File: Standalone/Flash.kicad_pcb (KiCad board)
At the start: 2 copper layers, 83.3 x 92.7 mm, 47 parts, among them CON1 GENESIS-CONN, J1 USB_B_Micro, U1 RT9193, U2 STM32F103C8Tx, U3 4069, U4 74HC590, U5 74LVC245, U6 74HC590, U7 74LVC245, U8 74HC590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

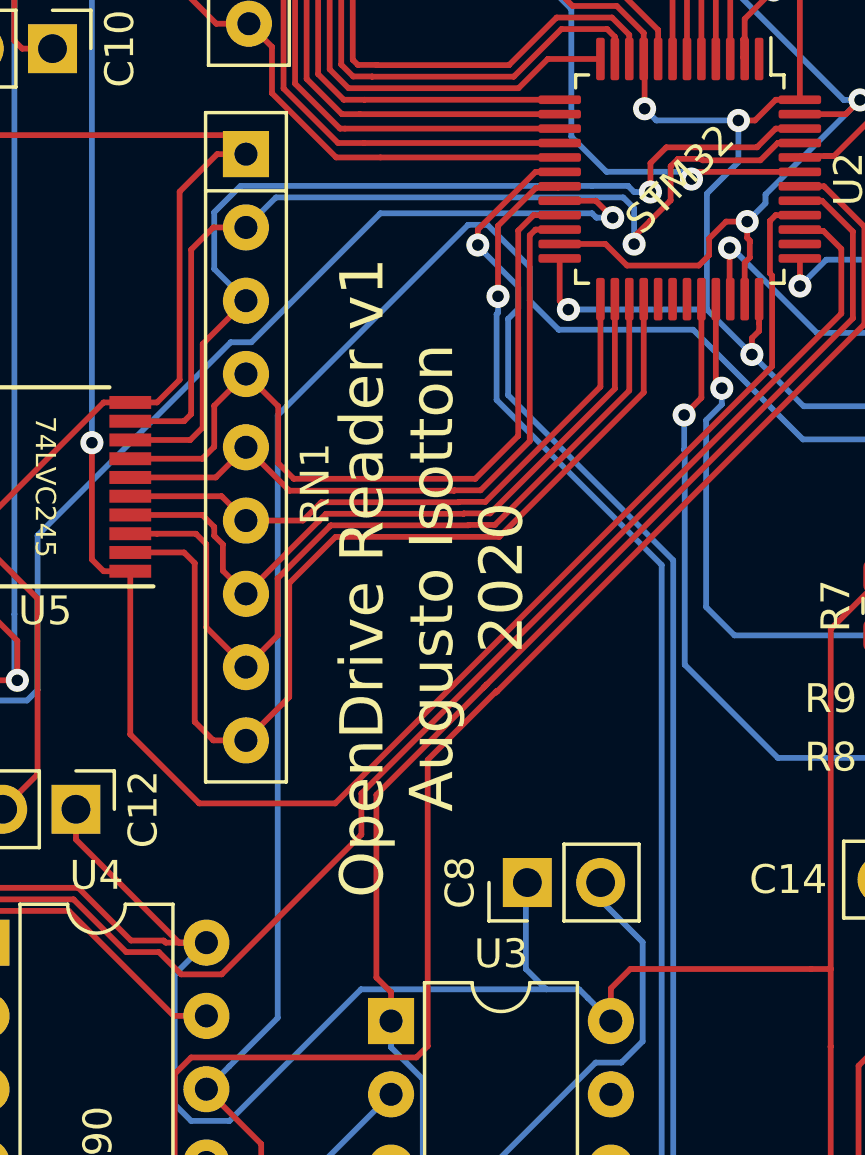
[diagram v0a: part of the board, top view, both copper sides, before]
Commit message: Small silkscreen changes
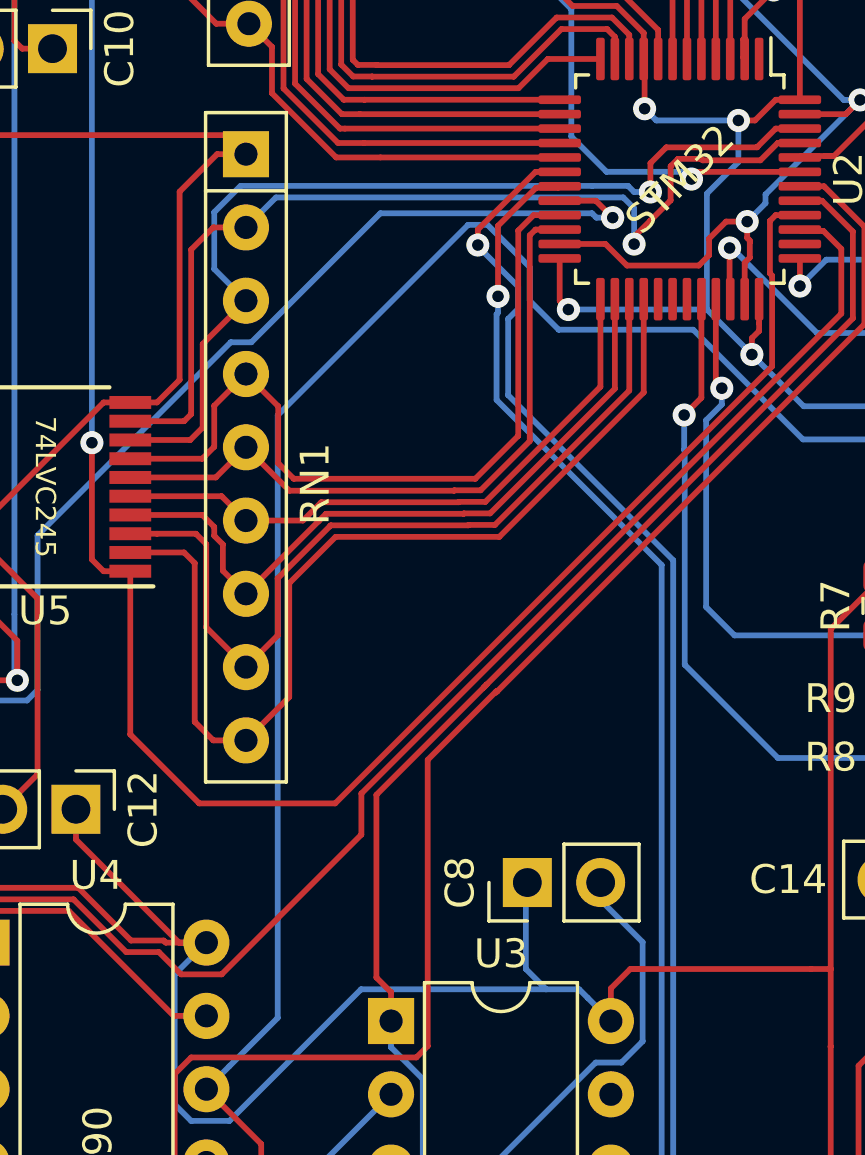
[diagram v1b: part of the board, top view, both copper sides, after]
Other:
- board text removed: "OpenDrive Reader v1 Augusto Isotton 2020"
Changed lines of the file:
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@@
   (general
     (thickness 1.6)
-    (drawings 28)
+    (drawings 27)
     (tracks 1703)
     (zones 0)
@@
     (effects (font (size 1 1) (thickness 0.15)))
   )
-  (gr_text "OpenDrive Reader v1\nAugusto Isotton\n2020" (at 136.5504 63.754 90) (layer F.SilkS)
-    (effects (font (size 1.5 1.5) (thickness 0.3)))
-  )
   (gr_text "GND\n" (at 98.6536 43.8912 90) (layer F.SilkS)

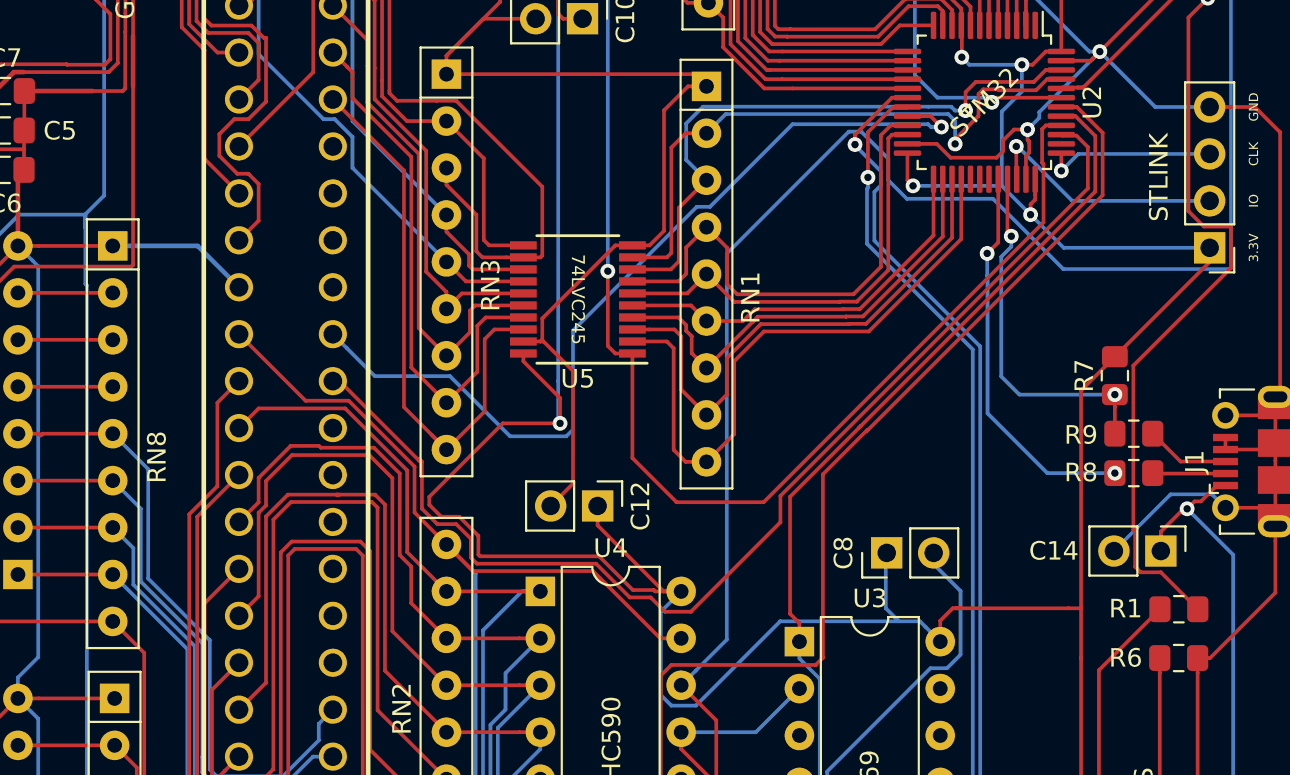
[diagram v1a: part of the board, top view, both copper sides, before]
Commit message: Connected A22 and A23 on the cart connector for SNES support
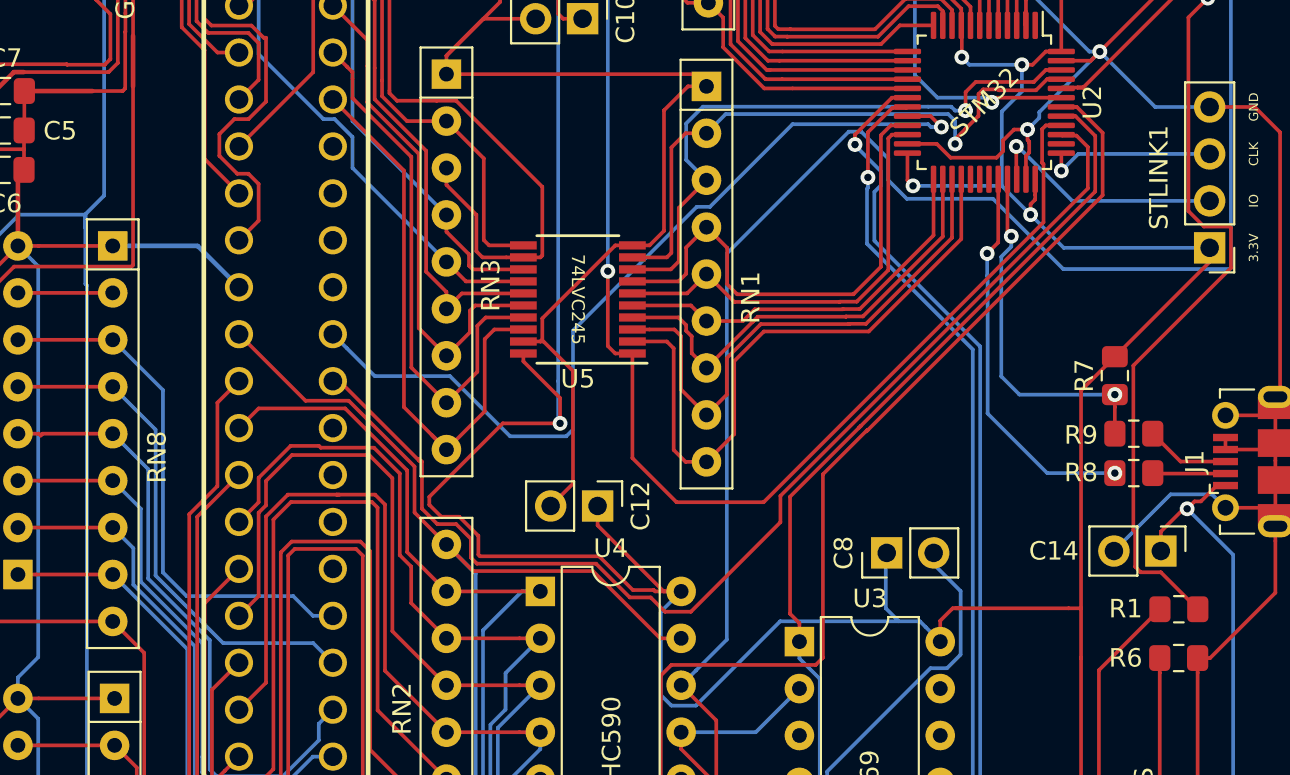
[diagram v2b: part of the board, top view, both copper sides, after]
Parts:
- renumbered STLINK to STLINK1
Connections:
- CON1 pad B10: (no net) -> /A21
- CON1 pad B11: (no net) -> /A22
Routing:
- net /A22: track 5.08 -> 29.0 mm
- net /A21: track 5.08 -> 27.8 mm
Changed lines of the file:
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@@
     (thickness 1.6)
     (drawings 27)
-    (tracks 1703)
+    (tracks 1714)
     (zones 0)
     (modules 47)
@@
   )
   (setup
-    (last_trace_width 0.25)
+    (last_trace_width 0.2)
     (user_trace_width 0.2)
     (user_trace_width 0.5)
@@
     (pad B9 thru_hole circle (at 0 20.32) (size 1.524 1.524) (drill 1.016) (layers *.Cu *.Mask)
       (net 28 /A20))
-    (pad B10 thru_hole circle (at 0 22.86) (size 1.524 1.524) (drill 1.016) (layers *.Cu *.Mask))
-    (pad B11 thru_hole circle (at 0 25.4) (size 1.524 1.524) (drill 1.016) (layers *.Cu *.Mask))
+    (pad B10 thru_hole circle (at 0 22.86) (size 1.524 1.524) (drill 1.016) (layers *.Cu *.Mask)
+      (net 76 /A21))
+    (pad B11 thru_hole circle (at 0 25.4) (size 1.524 1.524) (drill 1.016) (layers *.Cu *.Mask)
+      (net 77 /A22))
     (pad B12 thru_hole circle (at 0 27.94) (size 1.524 1.524) (drill 1.016) (layers *.Cu *.Mask))
     (pad B13 thru_hole circle (at 0 30.48) (size 1.524 1.524) (drill 1.016) (layers *.Cu *.Mask))
@@
     (descr "Through hole straight pin header, 1x04, 2.54mm pitch, single row")
     (tags "Through hole pin header THT 1x04 2.54mm single row")
-    (fp_text reference STLINK (at 2.7432 3.81 90) (layer F.SilkS)
+    (fp_text reference STLINK1 (at 2.7432 3.81 90) (layer F.SilkS)
       (effects (font (size 1 1) (thickness 0.15)))
     )
@@
   (segment (start 139.18561 57.42591) (end 144.908411 63.148711) (width 0.2) (layer B.Cu) (net 75))
   (segment (start 92.837 65.3288) (end 97.917 65.3288) (width 0.2) (layer F.Cu) (net 76) (status 30))
+  (segment (start 108.818399 79.201999) (end 109.8804 80.264) (width 0.2) (layer B.Cu) (net 76))
+  (segment (start 103.943792 79.201999) (end 108.818399 79.201999) (width 0.2) (layer B.Cu) (net 76))
+  (segment (start 100.28543 75.543637) (end 103.943792 79.201999) (width 0.2) (layer B.Cu) (net 76))
+  (segment (start 97.9678 65.3288) (end 100.28543 67.64643) (width 0.2) (layer B.Cu) (net 76))
+  (segment (start 100.28543 67.64643) (end 100.28543 75.543637) (width 0.2) (layer B.Cu) (net 76))
   (segment (start 92.837 62.7888) (end 97.917 62.7888) (width 0.2) (layer F.Cu) (net 77) (status 30))
+  (segment (start 108.80277 77.724) (end 107.73597 76.6572) (width 0.2) (layer B.Cu) (net 77))
+  (segment (start 109.8804 77.724) (end 108.80277 77.724) (width 0.2) (layer B.Cu) (net 77))
+  (segment (start 107.73597 76.6572) (end 101.964691 76.6572) (width 0.2) (layer B.Cu) (net 77))
+  (segment (start 101.964691 76.6572) (end 100.68544 75.377949) (width 0.2) (layer B.Cu) (net 77))
+  (segment (start 100.68544 65.50644) (end 97.9678 62.7888) (width 0.2) (layer B.Cu) (net 77))
+  (segment (start 100.68544 75.377949) (end 100.68544 65.50644) (width 0.2) (layer B.Cu) (net 77))
   (segment (start 92.837 60.2488) (end 97.917 60.2488) (width 0.2) (layer F.Cu) (net 78) (status 30))
   (via (at 146.8628 52.324) (size 0.8) (drill 0.4) (layers F.Cu B.Cu) (net 79))
